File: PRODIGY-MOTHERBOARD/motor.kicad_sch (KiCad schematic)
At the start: 4 parts, among them U12 DRV8870DDA

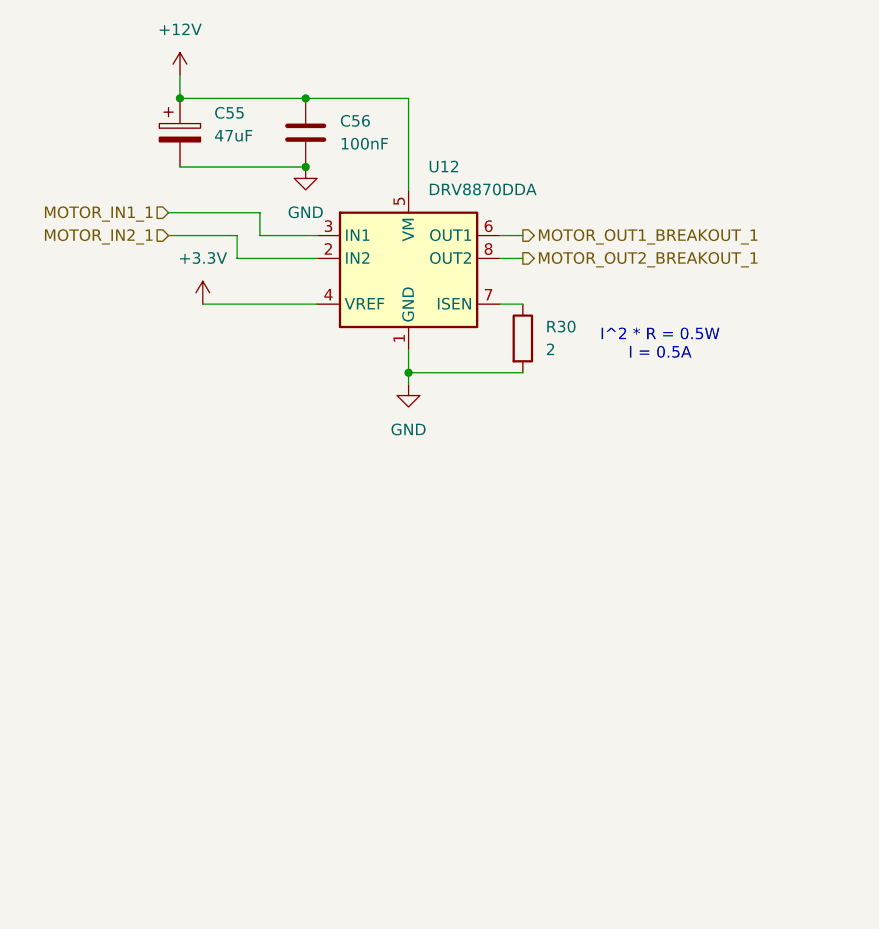
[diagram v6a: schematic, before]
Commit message: Submitted V0 for evaluation. Avaiting feedback.
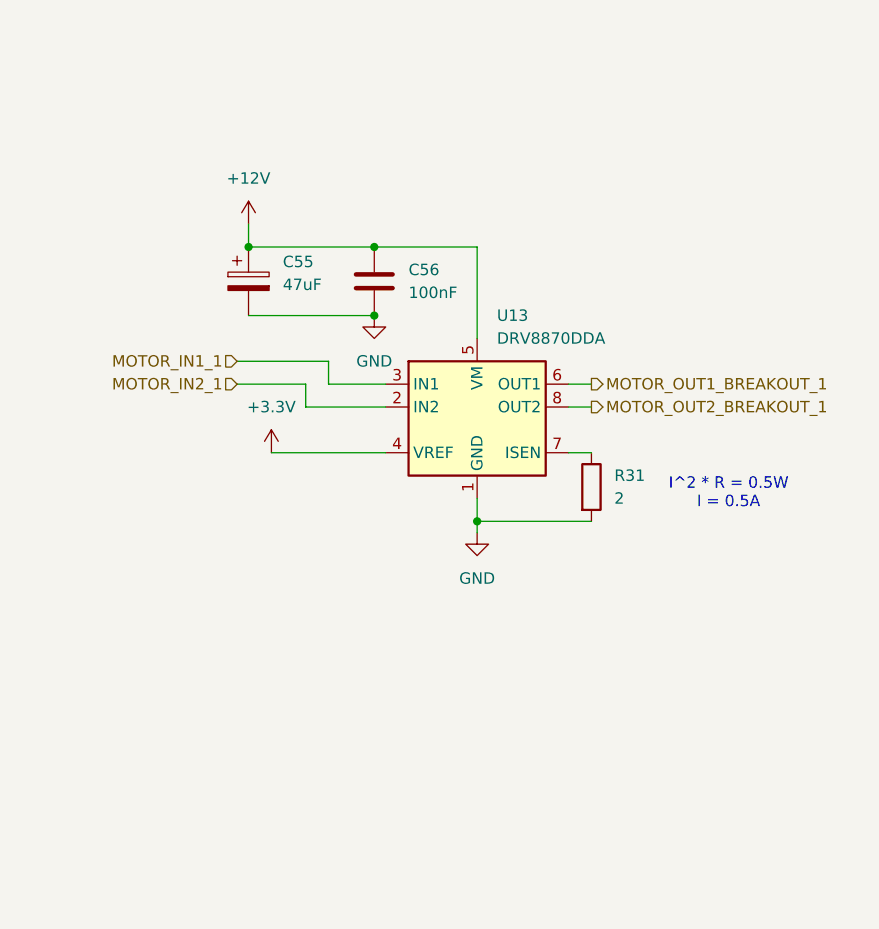
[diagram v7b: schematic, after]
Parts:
- renumbered R30 to R31, U12 to U13
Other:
- moved on the sheet: C55, C56, R31, U13

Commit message: Finished v0.1 schematic.
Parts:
- renumbered C55 to C33, C56 to C34, R31 to R25, U13 to U5
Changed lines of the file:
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@@
 		(dnp no)
 		(fields_autoplaced yes)
-		(property "Reference" "#PWR094"
+		(property "Reference" "#PWR065"
 			(at 120.65 77.47 0)
 			(effects
@@
 			(project "PRODIGY-MOTHERBOARD"
 				(path "/f1c25860-8989-4190-bd24-2491d23ca7d9/68c611b4-6626-4f5e-8db6-2b7527a0fa95"
-					(reference "#PWR094")
+					(reference "#PWR065")
 					(unit 1)
 				)
@@
 		(dnp no)
 		(fields_autoplaced yes)
-		(property "Reference" "R31"
+		(property "Reference" "R25"
 			(at 161.29 101.5999 0)
 			(effects
@@
 			(project "PRODIGY-MOTHERBOARD"
 				(path "/f1c25860-8989-4190-bd24-2491d23ca7d9/68c611b4-6626-4f5e-8db6-2b7527a0fa95"
-					(reference "R31")
+					(reference "R25")
 					(unit 1)
 				)
@@
 		(dnp no)
 		(fields_autoplaced yes)
-		(property "Reference" "#PWR097"
+		(property "Reference" "#PWR068"
 			(at 146.05 114.3 0)
 			(effects
@@
 			(project "PRODIGY-MOTHERBOARD"
 				(path "/f1c25860-8989-4190-bd24-2491d23ca7d9/68c611b4-6626-4f5e-8db6-2b7527a0fa95"
-					(reference "#PWR097")
+					(reference "#PWR068")
 					(unit 1)
 				)
@@
 		(dnp no)
 		(fields_autoplaced yes)
-		(property "Reference" "C55"
+		(property "Reference" "C33"
 			(at 124.46 77.8509 0)
 			(effects
@@
 			(project "PRODIGY-MOTHERBOARD"
 				(path "/f1c25860-8989-4190-bd24-2491d23ca7d9/68c611b4-6626-4f5e-8db6-2b7527a0fa95"
-					(reference "C55")
+					(reference "C33")
 					(unit 1)
 				)
@@
 		(dnp no)
 		(fields_autoplaced yes)
-		(property "Reference" "C56"
+		(property "Reference" "C34"
 			(at 138.43 78.7399 0)
 			(effects
@@
 			(project "PRODIGY-MOTHERBOARD"
 				(path "/f1c25860-8989-4190-bd24-2491d23ca7d9/68c611b4-6626-4f5e-8db6-2b7527a0fa95"
-					(reference "C56")
+					(reference "C34")
 					(unit 1)
 				)
@@
 		(dnp no)
 		(fields_autoplaced yes)
-		(property "Reference" "#PWR096"
+		(property "Reference" "#PWR066"
 			(at 123.19 102.87 0)
 			(effects
@@
 			(project "PRODIGY-MOTHERBOARD"
 				(path "/f1c25860-8989-4190-bd24-2491d23ca7d9/68c611b4-6626-4f5e-8db6-2b7527a0fa95"
-					(reference "#PWR096")
+					(reference "#PWR066")
 					(unit 1)
 				)
@@
 		(dnp no)
 		(fields_autoplaced yes)
-		(property "Reference" "#PWR095"
+		(property "Reference" "#PWR067"
 			(at 134.62 90.17 0)
 			(effects
@@
 			(project "PRODIGY-MOTHERBOARD"
 				(path "/f1c25860-8989-4190-bd24-2491d23ca7d9/68c611b4-6626-4f5e-8db6-2b7527a0fa95"
-					(reference "#PWR095")
+					(reference "#PWR067")
 					(unit 1)
 				)
@@
 		(dnp no)
 		(fields_autoplaced yes)
-		(property "Reference" "U13"
+		(property "Reference" "U5"
 			(at 148.2441 83.82 0)
 			(effects
@@
 			(project "PRODIGY-MOTHERBOARD"
 				(path "/f1c25860-8989-4190-bd24-2491d23ca7d9/68c611b4-6626-4f5e-8db6-2b7527a0fa95"
-					(reference "U13")
-					(unit 1)
-				)
+					(reference "U5")
+					(unit 1)
+				)
